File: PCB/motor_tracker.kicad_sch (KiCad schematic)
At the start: 0 parts

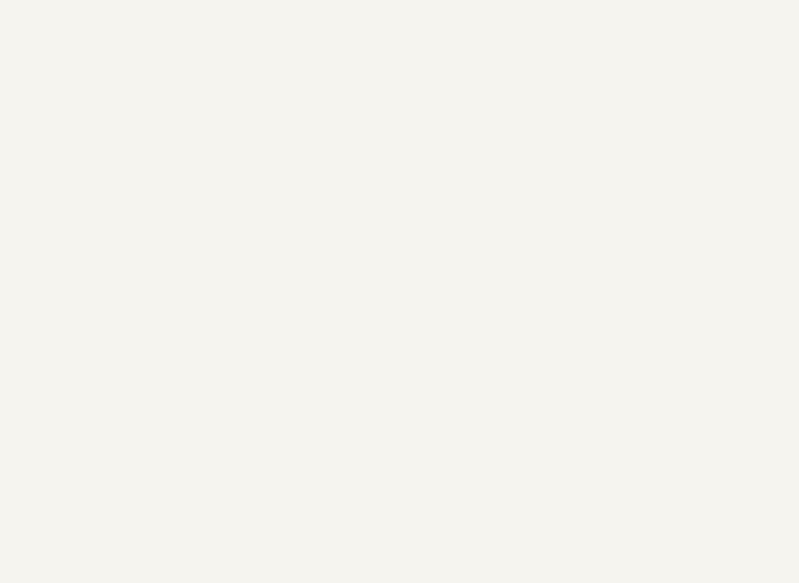
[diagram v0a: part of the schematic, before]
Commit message: Added USB connector
Added acceleration sensor

Added combined gyro and acceleration sensor
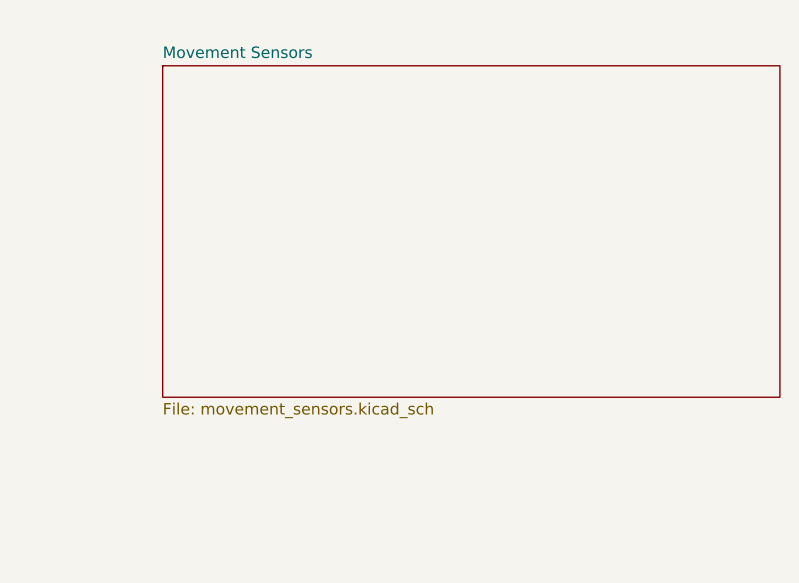
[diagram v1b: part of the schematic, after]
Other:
- added sheet Movement Sensors (movement_sensors.kicad_sch)
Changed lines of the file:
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@@
+    )
+  )
+  (sheet (at -106.68 -82.55) (size 68.58 36.83) (fields_autoplaced)
+    (stroke (width 0.1524) (type solid))
+    (fill (color 0 0 0 0.0000))
+    (property "Sheetname" "Movement Sensors" (at -106.68 -83.2616 0)
+      (effects (font (size 1.27 1.27)) (justify left bottom))
+    )
+    (property "Sheetfile" "movement_sensors.kicad_sch" (at -106.68 -45.1354 0)
+      (effects (font (size 1.27 1.27)) (justify left top))
+    )
+    (property "Field2" "" (at -106.68 -82.55 0)
+      (effects (font (size 1.27 1.27)) hide)
+    )
+    (instances
+      (project "motor_tracker"
+        (path "/a8928dcf-7fea-46f0-8c15-a3fa49b43e6b" (page "7"))
+      )
     )
   )

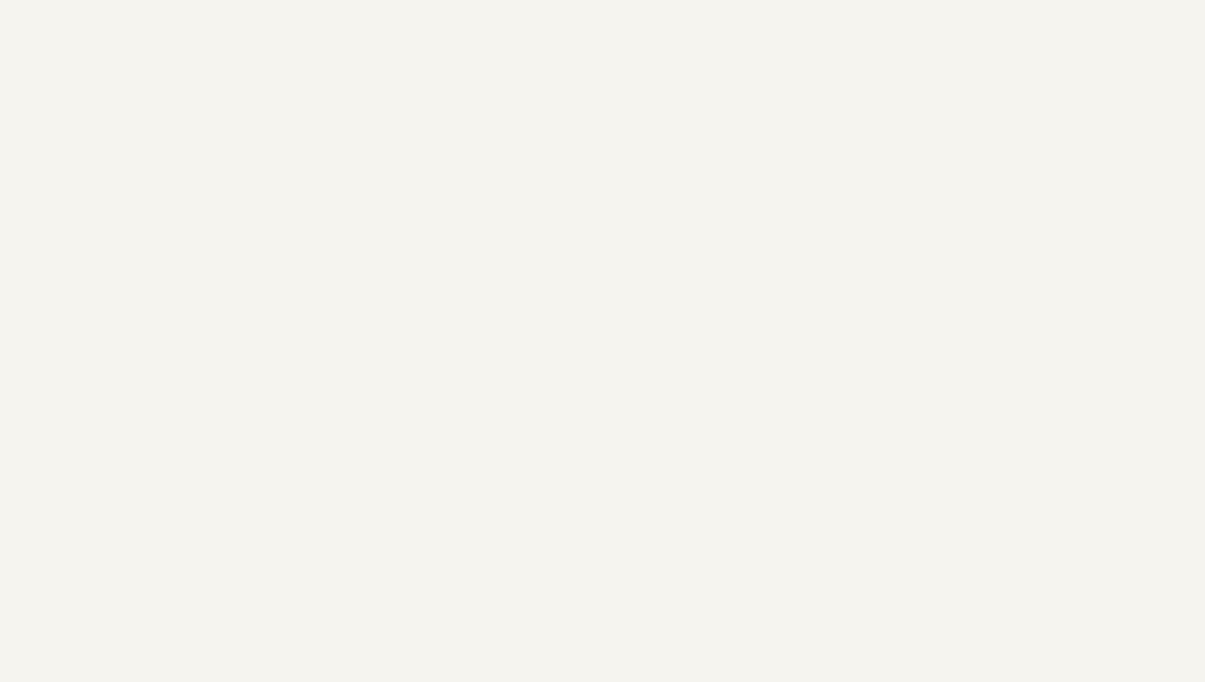
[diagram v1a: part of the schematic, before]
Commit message: Input voltage protection added
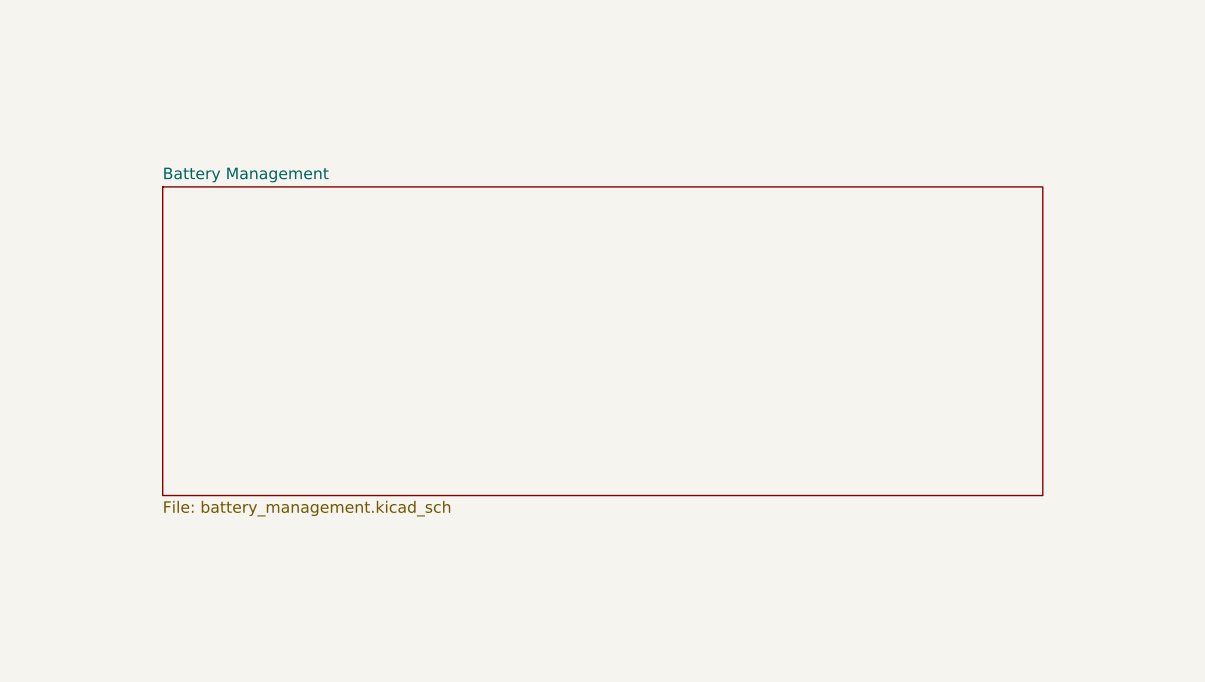
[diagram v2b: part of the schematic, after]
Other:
- added sheet Battery Management (battery_management.kicad_sch)
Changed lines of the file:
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@@
 (kicad_sch (version 20230121) (generator eeschema)
   (paper "A4")
+  (sheet (at -217.17 -20.32) (size 97.79 34.29) (fields_autoplaced)
+    (stroke (width 0.1524) (type solid))
+    (fill (color 0 0 0 0.0000))
+    (property "Sheetname" "Battery Management" (at -217.17 -21.0316 0)
+      (effects (font (size 1.27 1.27)) (justify left bottom))
+    )
+    (property "Sheetfile" "battery_management.kicad_sch" (at -217.17 14.5546 0)
+      (effects (font (size 1.27 1.27)) (justify left top))
+    )
+    (property "Field2" "" (at -217.17 -20.32 0)
+      (effects (font (size 1.27 1.27)) hide)
+    )
+    (instances
+      (project "motor_tracker"
+        (path "/a8928dcf-7fea-46f0-8c15-a3fa49b43e6b" (page "3"))
+      )
+    )
+  )
   (sheet (at -288.29 40.64) (size 71.12 30.48) (fields_autoplaced)
     (stroke (width 0.1524) (type solid))
@@
     (instances
       (project "motor_tracker"
-        (path "/a8928dcf-7fea-46f0-8c15-a3fa49b43e6b" (page "4"))
+        (path "/a8928dcf-7fea-46f0-8c15-a3fa49b43e6b" (page "6"))
       )
     )
@@
     (instances
       (project "motor_tracker"
-        (path "/a8928dcf-7fea-46f0-8c15-a3fa49b43e6b" (page "3"))
+        (path "/a8928dcf-7fea-46f0-8c15-a3fa49b43e6b" (page "4"))
       )
     )
@@
     (instances
       (project "motor_tracker"
-        (path "/a8928dcf-7fea-46f0-8c15-a3fa49b43e6b" (page "6"))
+        (path "/a8928dcf-7fea-46f0-8c15-a3fa49b43e6b" (page "7"))
       )
     )
@@
     (instances
       (project "motor_tracker"
-        (path "/a8928dcf-7fea-46f0-8c15-a3fa49b43e6b" (page "7"))
+        (path "/a8928dcf-7fea-46f0-8c15-a3fa49b43e6b" (page "8"))
       )
     )
